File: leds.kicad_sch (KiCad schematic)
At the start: 38 parts

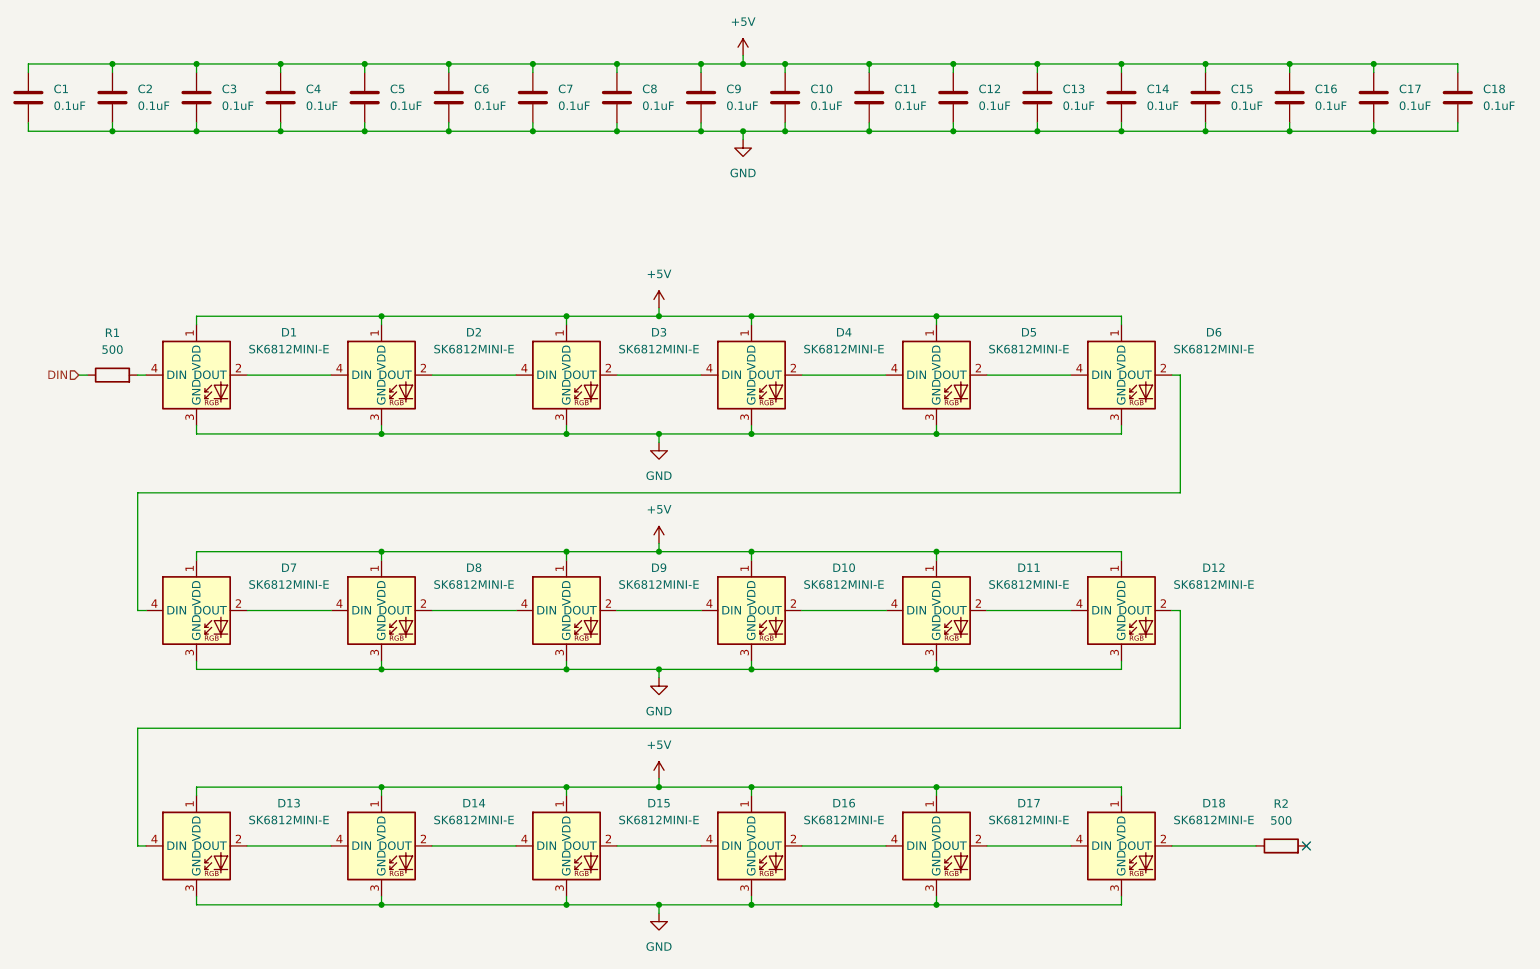
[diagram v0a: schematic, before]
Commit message: Fix symbols and footprints
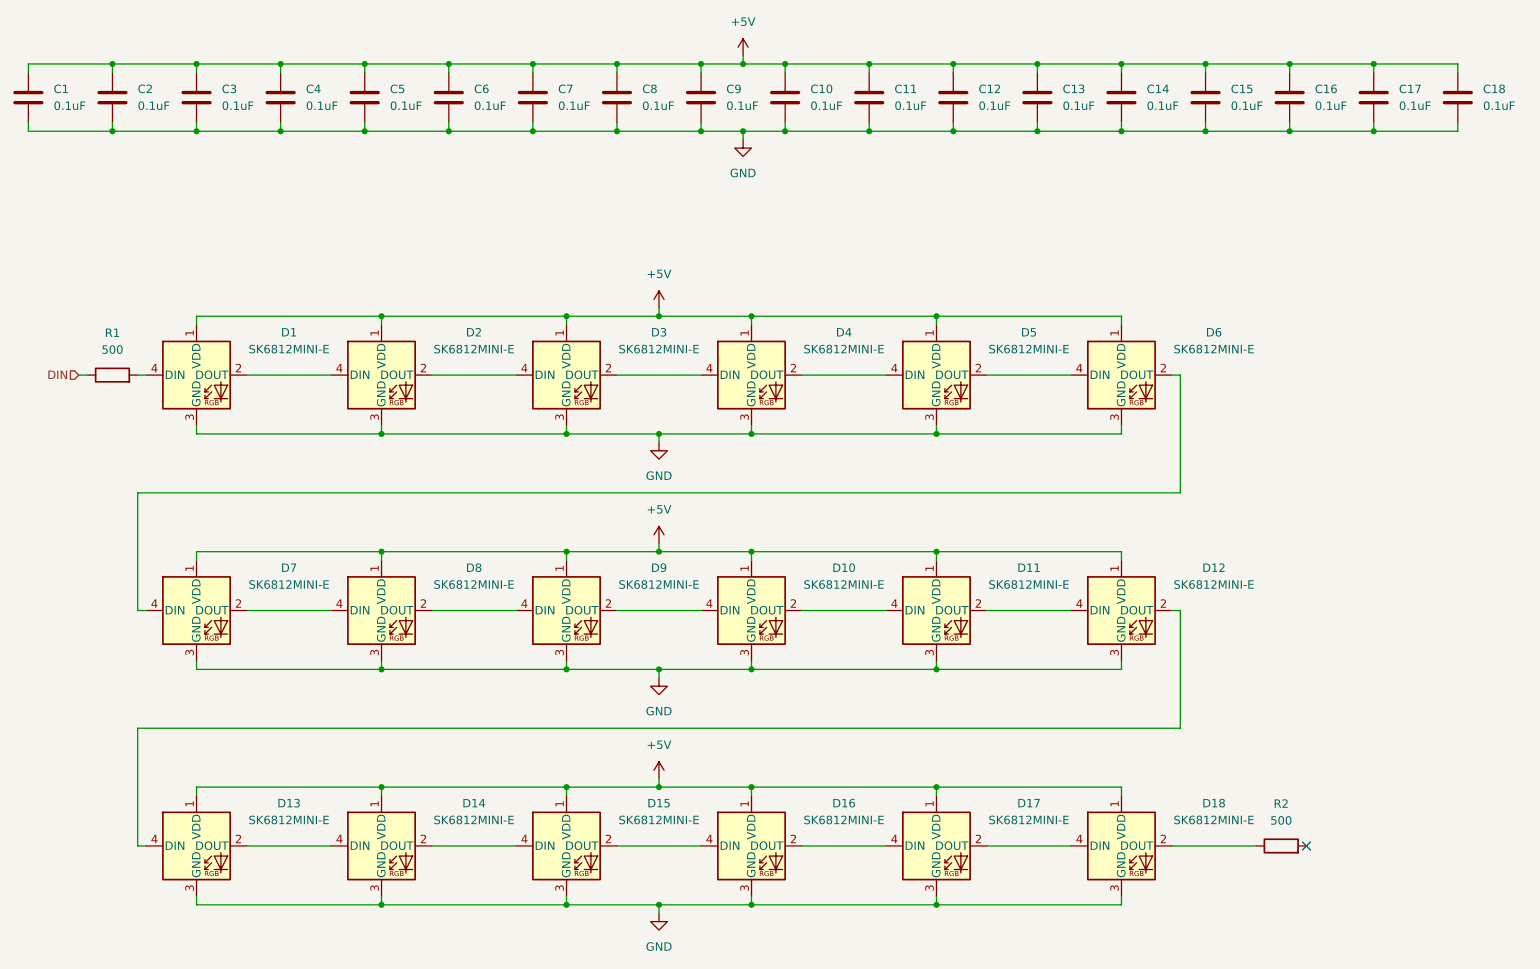
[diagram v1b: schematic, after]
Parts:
- D1, D10, D11, D12, D13, D14, D15, D16, D17, D18, D2, D3, D4, D5, D6, D7, D8, D9: footprint The_Crux:LED_SK6812MINI-E_PLCC4_3.2x2.8mm_P1.5mm_ReverseMount -> The_Crux:LED_SK6812MINI-E_PLCC4_3.2x2.8mm_P1.5mm_Reversible
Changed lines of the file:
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@@
 			)
 		)
-		(property "Footprint" "The_Crux:LED_SK6812MINI-E_PLCC4_3.2x2.8mm_P1.5mm_ReverseMount"
+		(property "Footprint" "The_Crux:LED_SK6812MINI-E_PLCC4_3.2x2.8mm_P1.5mm_Reversible"
 			(at 191.77 115.57 0)
 			(effects
@@
 			)
 		)
-		(property "Footprint" "The_Crux:LED_SK6812MINI-E_PLCC4_3.2x2.8mm_P1.5mm_ReverseMount"
+		(property "Footprint" "The_Crux:LED_SK6812MINI-E_PLCC4_3.2x2.8mm_P1.5mm_Reversible"
 			(at 191.77 151.13 0)
 			(effects
@@
 			)
 		)
-		(property "Footprint" "The_Crux:LED_SK6812MINI-E_PLCC4_3.2x2.8mm_P1.5mm_ReverseMount"
+		(property "Footprint" "The_Crux:LED_SK6812MINI-E_PLCC4_3.2x2.8mm_P1.5mm_Reversible"
 			(at 163.83 151.13 0)
 			(effects
@@
 			)
 		)
-		(property "Footprint" "The_Crux:LED_SK6812MINI-E_PLCC4_3.2x2.8mm_P1.5mm_ReverseMount"
+		(property "Footprint" "The_Crux:LED_SK6812MINI-E_PLCC4_3.2x2.8mm_P1.5mm_Reversible"
 			(at 191.77 80.01 0)
 			(effects
@@
 			)
 		)
-		(property "Footprint" "The_Crux:LED_SK6812MINI-E_PLCC4_3.2x2.8mm_P1.5mm_ReverseMount"
+		(property "Footprint" "The_Crux:LED_SK6812MINI-E_PLCC4_3.2x2.8mm_P1.5mm_Reversible"
 			(at 107.95 80.01 0)
 			(effects
@@
 			)
 		)
-		(property "Footprint" "The_Crux:LED_SK6812MINI-E_PLCC4_3.2x2.8mm_P1.5mm_ReverseMount"
+		(property "Footprint" "The_Crux:LED_SK6812MINI-E_PLCC4_3.2x2.8mm_P1.5mm_Reversible"
 			(at 52.07 80.01 0)
 			(effects
@@
 			)
 		)
-		(property "Footprint" "The_Crux:LED_SK6812MINI-E_PLCC4_3.2x2.8mm_P1.5mm_ReverseMount"
+		(property "Footprint" "The_Crux:LED_SK6812MINI-E_PLCC4_3.2x2.8mm_P1.5mm_Reversible"
 			(at 80.01 115.57 0)
 			(effects
@@
 			)
 		)
-		(property "Footprint" "The_Crux:LED_SK6812MINI-E_PLCC4_3.2x2.8mm_P1.5mm_ReverseMount"
+		(property "Footprint" "The_Crux:LED_SK6812MINI-E_PLCC4_3.2x2.8mm_P1.5mm_Reversible"
 			(at 163.83 80.01 0)
 			(effects
@@
 			)
 		)
-		(property "Footprint" "The_Crux:LED_SK6812MINI-E_PLCC4_3.2x2.8mm_P1.5mm_ReverseMount"
+		(property "Footprint" "The_Crux:LED_SK6812MINI-E_PLCC4_3.2x2.8mm_P1.5mm_Reversible"
 			(at 135.89 115.57 0)
 			(effects
@@
 			)
 		)
-		(property "Footprint" "The_Crux:LED_SK6812MINI-E_PLCC4_3.2x2.8mm_P1.5mm_ReverseMount"
+		(property "Footprint" "The_Crux:LED_SK6812MINI-E_PLCC4_3.2x2.8mm_P1.5mm_Reversible"
 			(at 52.07 115.57 0)
 			(effects
@@
 			)
 		)
-		(property "Footprint" "The_Crux:LED_SK6812MINI-E_PLCC4_3.2x2.8mm_P1.5mm_ReverseMount"
+		(property "Footprint" "The_Crux:LED_SK6812MINI-E_PLCC4_3.2x2.8mm_P1.5mm_Reversible"
 			(at 107.95 151.13 0)
 			(effects
@@
 			)
 		)
-		(property "Footprint" "The_Crux:LED_SK6812MINI-E_PLCC4_3.2x2.8mm_P1.5mm_ReverseMount"
+		(property "Footprint" "The_Crux:LED_SK6812MINI-E_PLCC4_3.2x2.8mm_P1.5mm_Reversible"
 			(at 107.95 115.57 0)
 			(effects
@@
 			)
 		)
-		(property "Footprint" "The_Crux:LED_SK6812MINI-E_PLCC4_3.2x2.8mm_P1.5mm_ReverseMount"
+		(property "Footprint" "The_Crux:LED_SK6812MINI-E_PLCC4_3.2x2.8mm_P1.5mm_Reversible"
 			(at 52.07 151.13 0)
 			(effects
@@
 			)
 		)
-		(property "Footprint" "The_Crux:LED_SK6812MINI-E_PLCC4_3.2x2.8mm_P1.5mm_ReverseMount"
+		(property "Footprint" "The_Crux:LED_SK6812MINI-E_PLCC4_3.2x2.8mm_P1.5mm_Reversible"
 			(at 80.01 80.01 0)
 			(effects
@@
 			)
 		)
-		(property "Footprint" "The_Crux:LED_SK6812MINI-E_PLCC4_3.2x2.8mm_P1.5mm_ReverseMount"
+		(property "Footprint" "The_Crux:LED_SK6812MINI-E_PLCC4_3.2x2.8mm_P1.5mm_Reversible"
 			(at 135.89 80.01 0)
 			(effects
@@
 			)
 		)
-		(property "Footprint" "The_Crux:LED_SK6812MINI-E_PLCC4_3.2x2.8mm_P1.5mm_ReverseMount"
+		(property "Footprint" "The_Crux:LED_SK6812MINI-E_PLCC4_3.2x2.8mm_P1.5mm_Reversible"
 			(at 163.83 115.57 0)
 			(effects
@@
 			)
 		)
-		(property "Footprint" "The_Crux:LED_SK6812MINI-E_PLCC4_3.2x2.8mm_P1.5mm_ReverseMount"
+		(property "Footprint" "The_Crux:LED_SK6812MINI-E_PLCC4_3.2x2.8mm_P1.5mm_Reversible"
 			(at 80.01 151.13 0)
 			(effects
@@
 			)
 		)
-		(property "Footprint" "The_Crux:LED_SK6812MINI-E_PLCC4_3.2x2.8mm_P1.5mm_ReverseMount"
+		(property "Footprint" "The_Crux:LED_SK6812MINI-E_PLCC4_3.2x2.8mm_P1.5mm_Reversible"
 			(at 135.89 151.13 0)
 			(effects
